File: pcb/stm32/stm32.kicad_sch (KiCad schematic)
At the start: 1 part

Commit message: Preparing schema
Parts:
- removed U?: STM32G070KBT6, LQFP-32, symbol 2023-02-12_17-09-08:STM32G070KBT6
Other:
- added sheet stm32_core (stm32_core.kicad_sch)
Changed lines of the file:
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@@
 (kicad_sch (version 20211123) (generator eeschema)
   (paper "A4")
-  (symbol (lib_id "2023-02-12_17-09-08:STM32G070KBT6") (at 111.76 46.99 0) (unit 1)
-    (in_bom yes) (on_board yes) (fields_autoplaced)
-    (property "Reference" "U?" (id 0) (at 144.78 35.56 0)
-      (effects (font (size 1.524 1.524)))
+  (sheet (at 39.37 31.75) (size 33.02 25.4) (fields_autoplaced)
+    (stroke (width 0.1524) (type solid) (color 0 0 0 0))
+    (fill (color 0 0 0 0.0000))
+    (property "Sheet name" "stm32_core" (id 0) (at 39.37 31.0384 0)
+      (effects (font (size 1.27 1.27)) (justify left bottom))
     )
-    (property "Value" "STM32G070KBT6" (id 1) (at 144.78 39.37 0)
-      (effects (font (size 1.524 1.524)))
+    (property "Sheet file" "stm32_core.kicad_sch" (id 1) (at 39.37 57.7346 0)
+      (effects (font (size 1.27 1.27)) (justify left top))
     )
-    (property "Footprint" "LQFP-32" (id 2) (at 111.76 46.99 0)
-      (effects (font (size 1.27 1.27) italic) hide)
-    )
-    (property "Datasheet" "STM32G070KBT6" (id 3) (at 111.76 46.99 0)
-      (effects (font (size 1.27 1.27) italic) hide)
-    )
-    (pin "1")
-    (pin "10")
-    (pin "11")
-    (pin "12")
-    (pin "13")
-    (pin "14")
-    (pin "15")
-    (pin "16")
-    (pin "17")
-    (pin "18")
-    (pin "19")
-    (pin "2")
-    (pin "20")
-    (pin "21")
-    (pin "22")
-    (pin "23")
-    (pin "24")
-    (pin "25")
-    (pin "26")
-    (pin "27")
-    (pin "28")
-    (pin "29")
-    (pin "3")
-    (pin "30")
-    (pin "31")
-    (pin "32")
-    (pin "4")
-    (pin "5")
-    (pin "6")
-    (pin "7")
-    (pin "8")
-    (pin "9")
   )
   (sheet_instances
     (path "/" (page "1"))
+    (path "/9c894778-166f-4de3-959c-ace11ceeac49" (page "2"))
   )
   (symbol_instances
-    (path "/f794ca32-feeb-4763-ba7d-84693830793a"
+    (path "/9c894778-166f-4de3-959c-ace11ceeac49/6ffaf4d2-84ae-49da-99af-f19eadcc7714"
+      (reference "#PWR?") (unit 1) (value "GND") (footprint "")
+    )
+    (path "/9c894778-166f-4de3-959c-ace11ceeac49/ef05f5d4-ec6a-4157-ba22-e69a2151ac2a"
+      (reference "#PWR?") (unit 1) (value "+3.3V") (footprint "")
+    )
+    (path "/9c894778-166f-4de3-959c-ace11ceeac49/b684f68b-0d98-43b6-b962-3fdeb81b8baf"
       (reference "U?") (unit 1) (value "STM32G070KBT6") (footprint "LQFP-32")
     )

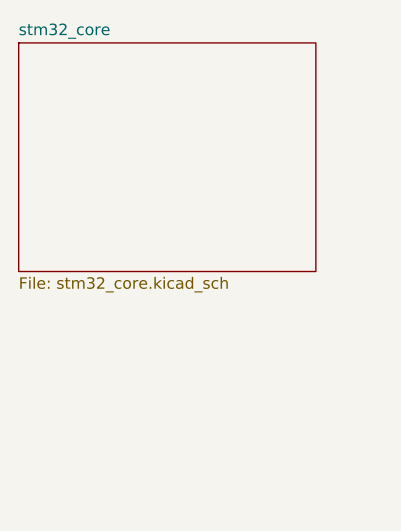
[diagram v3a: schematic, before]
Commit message: Added all hiearchical labels
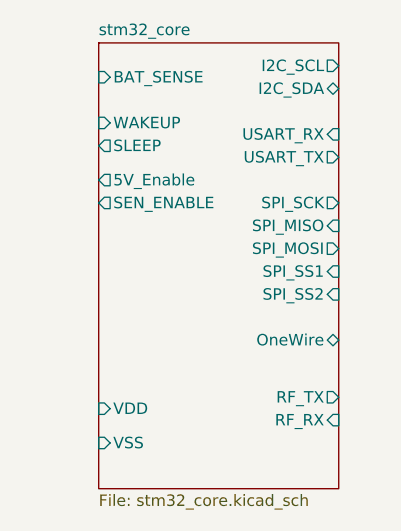
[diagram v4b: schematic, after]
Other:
- sheet stm32_core ports: added 5V_Enable, BAT_SENSE, I2C_SCL, I2C_SDA, OneWire, RF_RX, RF_TX, SEN_ENABLE, SLEEP, SPI_MISO, SPI_MOSI, SPI_SCK, SPI_SS1, SPI_SS2, USART_RX, USART_TX, VDD, VSS, WAKEUP; removed none
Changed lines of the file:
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@@
 (kicad_sch (version 20230121) (generator eeschema)
   (paper "A4")
-  (sheet (at 39.37 31.75) (size 33.02 25.4) (fields_autoplaced)
+  (sheet (at 48.26 31.75) (size 26.67 49.53) (fields_autoplaced)
     (stroke (width 0.1524) (type solid))
     (fill (color 0 0 0 0.0000))
-    (property "Sheetname" "stm32_core" (at 39.37 31.0384 0)
+    (property "Sheetname" "stm32_core" (at 48.26 31.0384 0)
       (effects (font (size 1.27 1.27)) (justify left bottom))
     )
-    (property "Sheetfile" "stm32_core.kicad_sch" (at 39.37 57.7346 0)
+    (property "Sheetfile" "stm32_core.kicad_sch" (at 48.26 81.8646 0)
       (effects (font (size 1.27 1.27)) (justify left top))
     )
+    (pin "I2C_SCL" output (at 74.93 34.29 0)
+      (effects (font (size 1.27 1.27)) (justify right))
+    )
+    (pin "SPI_MOSI" output (at 74.93 54.61 0)
+      (effects (font (size 1.27 1.27)) (justify right))
+    )
+    (pin "VSS" input (at 48.26 76.2 180)
+      (effects (font (size 1.27 1.27)) (justify left))
+    )
+    (pin "VDD" input (at 48.26 72.39 180)
+      (effects (font (size 1.27 1.27)) (justify left))
+    )
+    (pin "I2C_SDA" bidirectional (at 74.93 36.83 0)
+      (effects (font (size 1.27 1.27)) (justify right))
+    )
+    (pin "RF_RX" input (at 74.93 73.66 0)
+      (effects (font (size 1.27 1.27)) (justify right))
+    )
+    (pin "USART_TX" output (at 74.93 44.45 0)
+      (effects (font (size 1.27 1.27)) (justify right))
+    )
+    (pin "USART_RX" input (at 74.93 41.91 0)
+      (effects (font (size 1.27 1.27)) (justify right))
+    )
+    (pin "SPI_MISO" input (at 74.93 52.07 0)
+      (effects (font (size 1.27 1.27)) (justify right))
+    )
+    (pin "SEN_ENABLE" output (at 48.26 49.53 180)
+      (effects (font (size 1.27 1.27)) (justify left))
+    )
+    (pin "SLEEP" output (at 48.26 43.18 180)
+      (effects (font (size 1.27 1.27)) (justify left))
+    )
+    (pin "RF_TX" output (at 74.93 71.12 0)
+      (effects (font (size 1.27 1.27)) (justify right))
+    )
+    (pin "WAKEUP" input (at 48.26 40.64 180)
+      (effects (font (size 1.27 1.27)) (justify left))
+    )
+    (pin "SPI_SCK" output (at 74.93 49.53 0)
+      (effects (font (size 1.27 1.27)) (justify right))
+    )
+    (pin "BAT_SENSE" input (at 48.26 35.56 180)
+      (effects (font (size 1.27 1.27)) (justify left))
+    )
+    (pin "OneWire" tri_state (at 74.93 64.77 0)
+      (effects (font (size 1.27 1.27)) (justify right))
+    )
+    (pin "5V_Enable" output (at 48.26 46.99 180)
+      (effects (font (size 1.27 1.27)) (justify left))
+    )
+    (pin "SPI_SS1" input (at 74.93 57.15 0)
+      (effects (font (size 1.27 1.27)) (justify right))
+    )
+    (pin "SPI_SS2" input (at 74.93 59.69 0)
+      (effects (font (size 1.27 1.27)) (justify right))
+    )
     (instances

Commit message: Prepare for other components
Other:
- added sheet components_spi (components_spi.kicad_sch)
- added sheet power_supply (power_supply.kicad_sch)
- added sheet sensors_i2c (sensors_i2c.kicad_sch)
- added sheet sensors_onewire (sensors_onewire.kicad_sch)
- added sheet wireless (wireless.kicad_sch)
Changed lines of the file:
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@@
 (kicad_sch (version 20230121) (generator eeschema)
   (paper "A4")
+  (sheet (at 106.68 33.02) (size 19.05 11.43) (fields_autoplaced)
+    (stroke (width 0.1524) (type solid))
+    (fill (color 0 0 0 0.0000))
+    (property "Sheetname" "sensors_onewire" (at 106.68 32.3084 0)
+      (effects (font (size 1.27 1.27)) (justify left bottom))
+    )
+    (property "Sheetfile" "sensors_onewire.kicad_sch" (at 106.68 45.0346 0)
+      (effects (font (size 1.27 1.27)) (justify left top))
+    )
+    (instances
+      (project "stm32"
+        (path "/cc56704c-71b4-401e-bec6-203f83946289" (page "3"))
+      )
+    )
+  )
+  (sheet (at 85.09 99.06) (size 25.4 20.32) (fields_autoplaced)
+    (stroke (width 0.1524) (type solid))
+    (fill (color 0 0 0 0.0000))
+    (property "Sheetname" "sensors_i2c" (at 85.09 98.3484 0)
+      (effects (font (size 1.27 1.27)) (justify left bottom))
+    )
+    (property "Sheetfile" "sensors_i2c.kicad_sch" (at 85.09 119.9646 0)
+      (effects (font (size 1.27 1.27)) (justify left top))
+    )
+    (instances
+      (project "stm32"
+        (path "/cc56704c-71b4-401e-bec6-203f83946289" (page "5"))
+      )
+    )
+  )
+  (sheet (at 152.4 43.18) (size 29.21 26.67) (fields_autoplaced)
+    (stroke (width 0.1524) (type solid))
+    (fill (color 0 0 0 0.0000))
+    (property "Sheetname" "wireless" (at 152.4 42.4684 0)
+      (effects (font (size 1.27 1.27)) (justify left bottom))
+    )
+    (property "Sheetfile" "wireless.kicad_sch" (at 152.4 70.4346 0)
+      (effects (font (size 1.27 1.27)) (justify left top))
+    )
+    (instances
+      (project "stm32"
+        (path "/cc56704c-71b4-401e-bec6-203f83946289" (page "7"))
+      )
+    )
+  )
+  (sheet (at 106.68 62.23) (size 22.86 20.32) (fields_autoplaced)
+    (stroke (width 0.1524) (type solid))
+    (fill (color 0 0 0 0.0000))
+    (property "Sheetname" "power_supply" (at 106.68 61.5184 0)
+      (effects (font (size 1.27 1.27)) (justify left bottom))
+    )
+    (property "Sheetfile" "power_supply.kicad_sch" (at 106.68 83.1346 0)
+      (effects (font (size 1.27 1.27)) (justify left top))
+    )
+    (instances
+      (project "stm32"
+        (path "/cc56704c-71b4-401e-bec6-203f83946289" (page "4"))
+      )
+    )
+  )
   (sheet (at 48.26 31.75) (size 26.67 49.53) (fields_autoplaced)
     (stroke (width 0.1524) (type solid))
@@
       )
     )
+  )
+  (sheet (at 130.81 100.33) (size 21.59 19.05) (fields_autoplaced)
+    (stroke (width 0.1524) (type solid))
+    (fill (color 0 0 0 0.0000))
+    (property "Sheetname" "components_spi" (at 130.81 99.6184 0)
+      (effects (font (size 1.27 1.27)) (justify left bottom))
+    )
+    (property "Sheetfile" "components_spi.kicad_sch" (at 130.81 119.9646 0)
+      (effects (font (size 1.27 1.27)) (justify left top))
+    )
+    (instances
+      (project "stm32"
+        (path "/cc56704c-71b4-401e-bec6-203f83946289" (page "6"))
+      )
+    )

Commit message: Power supply
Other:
- added sheet USB (usb.kicad_sch)
- sheet power_supply ports: added 5V, 5V_Enable, GND, VBAT_SENSE, VDD; removed none

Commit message: Moved PCB forwar
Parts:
- added C6 (x2): 100n, symbol Device:C
- added C6: 10u, symbol Device:C
- added J12: Conn_01x02_Pin, symbol Connector:Conn_01x02_Pin
- added R3 (x2): 10K, symbol Device:R
- added U3: 24AA02-OT, Package_TO_SOT_SMD:SOT-23-5, symbol Memory_EEPROM:24AA02-OT
- added U4: TPS2041B, Package_TO_SOT_SMD:SOT-23-5, symbol Power_Management:TPS2041B
- added U5: 23A256, Package_SO:SOIC-8_3.9x4.9mm_P1.27mm, symbol Memory_EEPROM:M95256-WMN6P
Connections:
- net +3.3V: now also C6.1, J12.1 (Pin_1), R3.1, R3.1, U3.4 (V_{CC}), U4.5 (IN), U5.7 (~{HOLD}), U5.8 (VCC)
- net GND: now also C6.2, C6.2, C6.2, U3.2 (V_{SS}), U3.5 (WP), U4.2 (GND), U5.4 (VSS)
- new net: R3.2, U4.3 (~{OC})
- new net I2C_SCL: U3.1 (SCL)
- new net I2C_SDA: U3.3 (SDA)
- new net SENSOR_VDD: C6.1, C6.1, U4.1 (OUT)
- new net SEN_ENABLE: R3.2, U4.4 (~{EN})
- new net SPI_MISO: U5.2 (Q)
- new net SPI_MOSI: U5.5 (D)
- new net SPI_SCK: U5.6 (C)
- new net SPI_SS1: U5.1 (~{S})
- new net stm32_core/VDD: J12.2 (Pin_2)
- no-connect marks 0 -> 3
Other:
- removed sheet components_spi
- sheet USB ports: added GND, RX, TX, VDD; removed none
- sheet sensors_i2c ports: added GND, I2C_SCL, I2C_SDA, VDD; removed none
- sheet sensors_onewire ports: added GND, OneWire, VDD; removed none
- sheet stm32_core ports: added none; removed SPI_SS2
- sheet wireless ports: added GND, RF_RX, RF_TX, VDD; removed none
- note added: "EEPROM"
- note added: "Memory"
- note added: "SENSORS Switch"

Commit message: Packages
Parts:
- C6: footprint (none) -> Capacitor_SMD:C_0201_0603Metric
- C6: footprint (none) -> Capacitor_SMD:C_0805_2012Metric
- J12: footprint (none) -> Connector_PinHeader_2.00mm:PinHeader_1x02_P2.00mm_Vertical
- R3: footprint (none) -> Resistor_SMD:R_1206_3216Metric
- renumbered U3 to U1, U5 to U2, U4 to U3
